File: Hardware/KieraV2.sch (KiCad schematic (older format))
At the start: 19 parts, among them SW1 SW_Rotary1x4, SW2 SW_Rotary1x4, SW3 SW_Push, SW4 SW_Push, SW5 SW_Push

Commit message: added .gitignore, SW_rotary_2x4
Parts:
- removed SW1, SW2: SW_Rotary1x4, symbol Switch:SW_Rotary1x4
- added J1: Conn_01x06_Male, symbol Connector:Conn_01x06_Male
- added SW1, SW2: SW_Rotary2x4, symbol Switch:SW_Rotary2x4
- R1, R6: value 56 -> 150
- R2, R7: value 330 -> 680
- R3, R8: value 680 -> 1k97
- R4, R9: value 2k7 -> 22k
- U?: symbol STM32L4P5RET6:STM32L4P5RET6 -> KieraV2-rescue:STM32L4P5RET6-STM32L4P5RET6
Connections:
- net labels added: TODO
- wire segments 55 -> 63
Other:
- moved on the sheet: R1, R10, R11, R12, R13, R2, R3, R4, R5, R6, R7, R8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

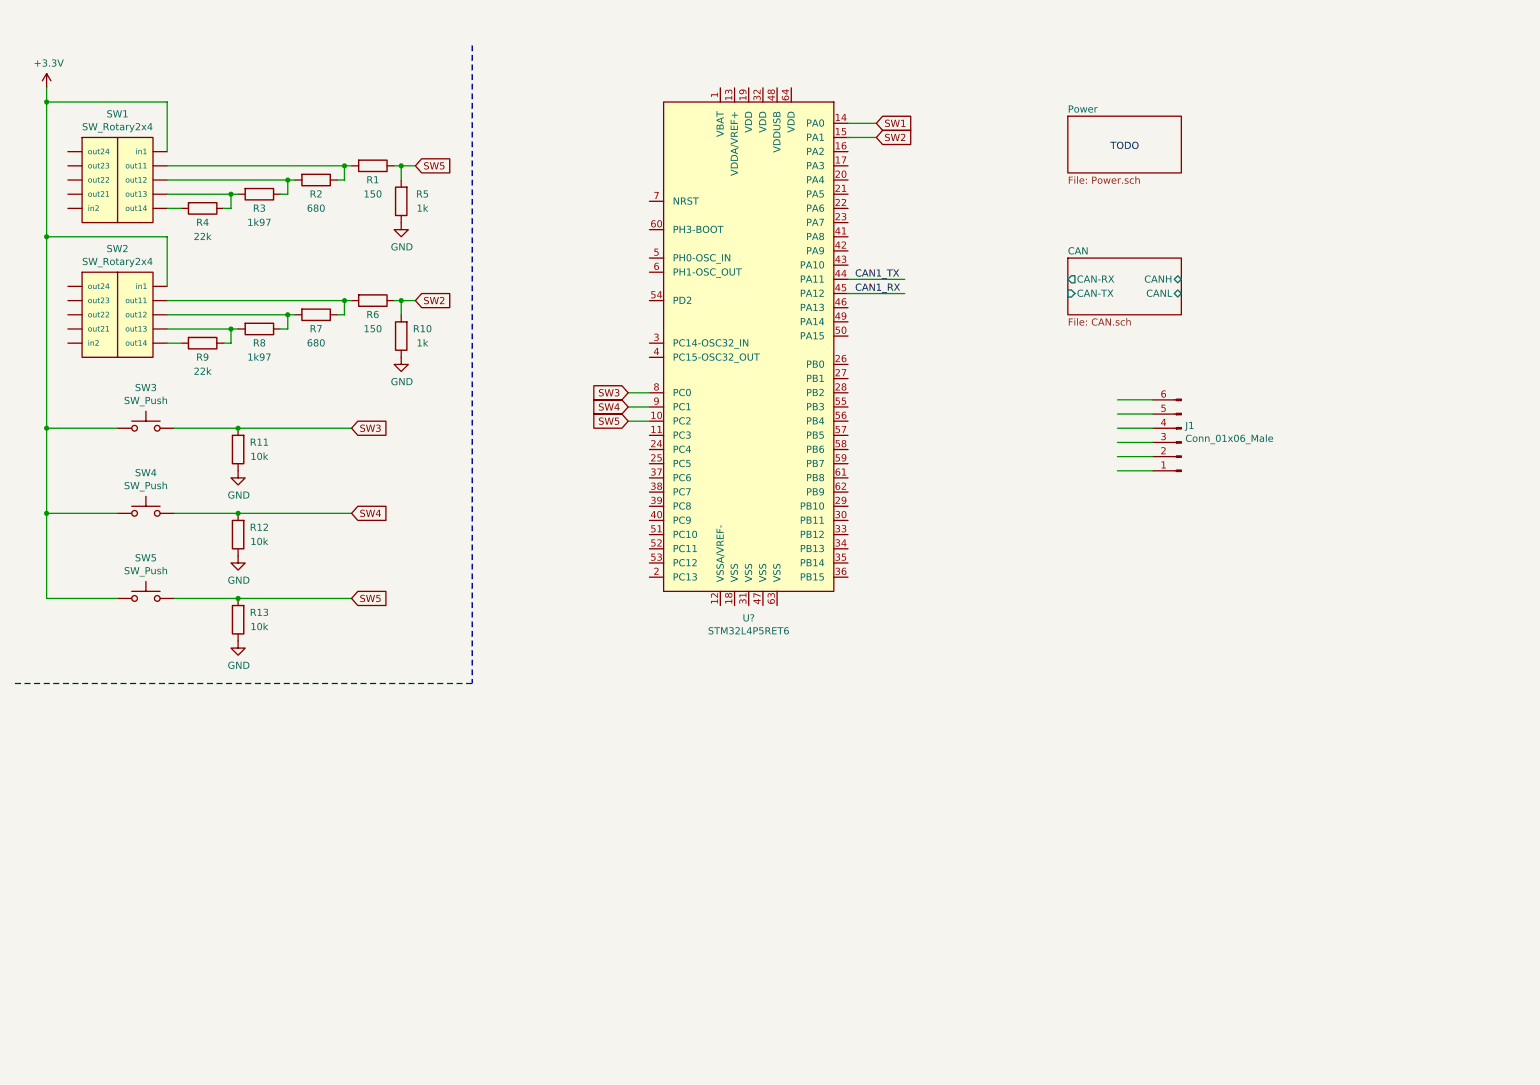
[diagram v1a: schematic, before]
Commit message: added SWD pinout
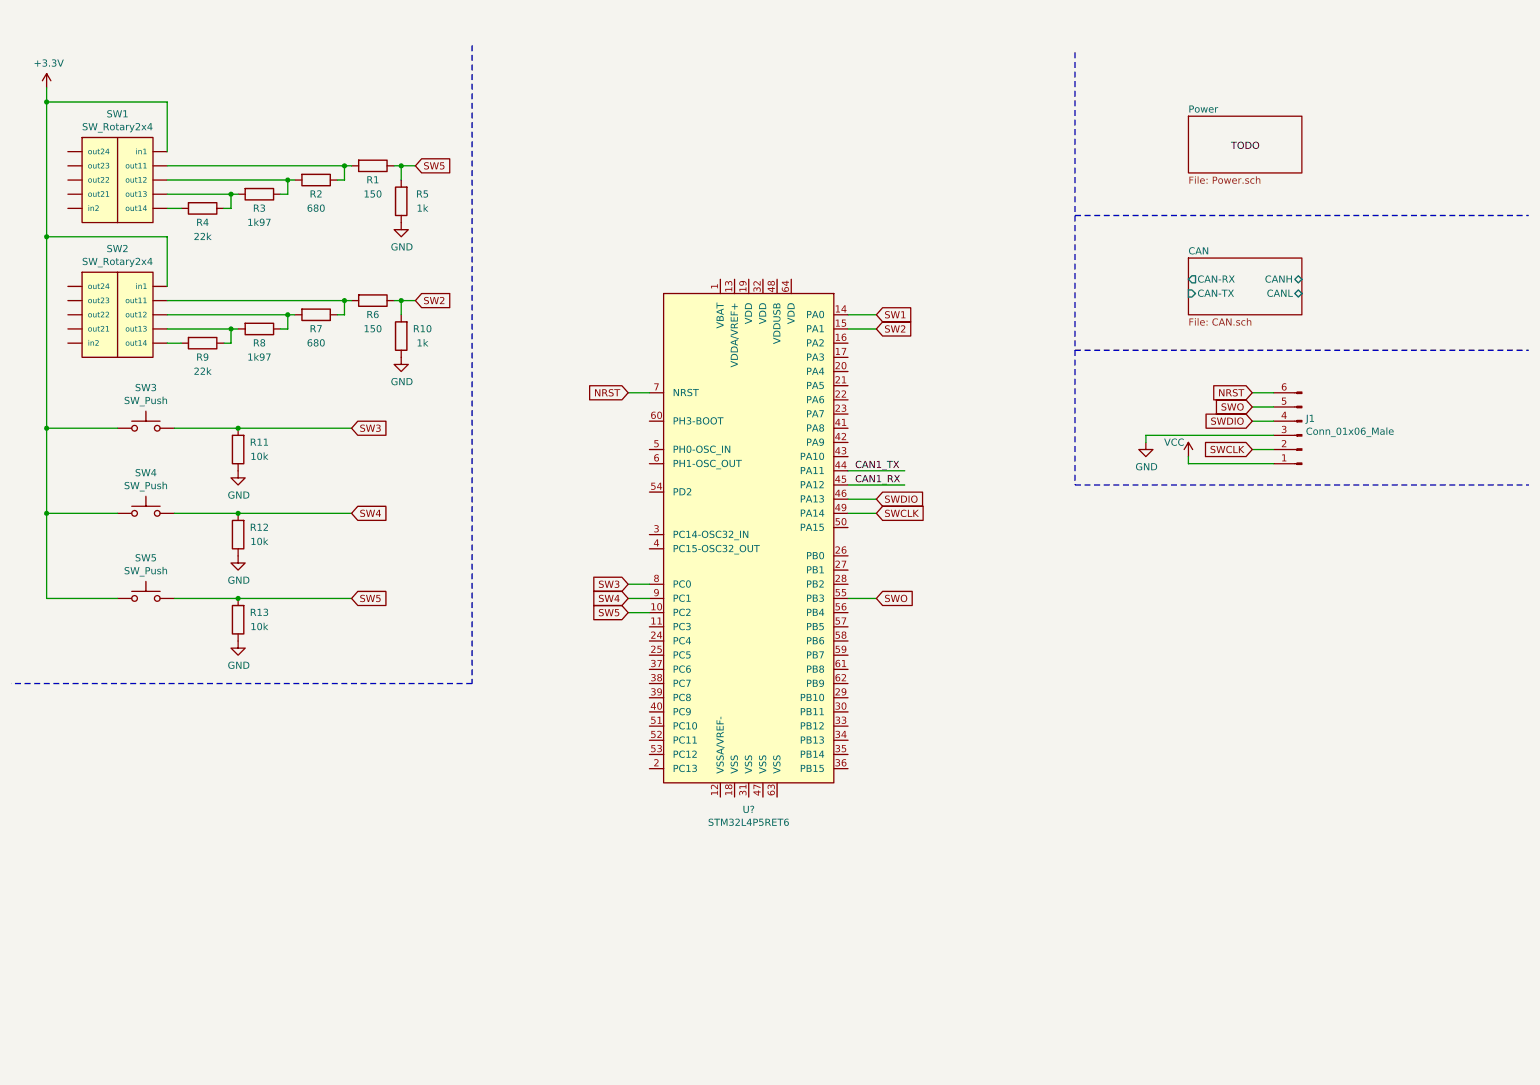
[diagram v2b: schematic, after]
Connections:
- net labels added: NRST, SWCLK, SWDIO, SWO, VCC
- wire segments 63 -> 69
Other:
- moved on the sheet: J1, U?
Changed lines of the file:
@@
 L KieraV2-rescue:STM32L4P5RET6-STM32L4P5RET6 U?
 U 1 1 619BCA75
-P 5700 2550
-F 0 "U?" H 5700 561 50  0000 C CNN
-F 1 "STM32L4P5RET6" H 5700 470 50  0000 C CNN
-F 2 "Package_QFP:LQFP-64_10x10mm_P0.5mm" H 5700 350 50  0001 C CNN
-F 3 "https://www.st.com/en/microcontrollers-microprocessors/stm32l4p5re.html#documentation" H 5700 350 50  0001 C CNN
-	1    5700 2550
+P 5700 3900
+F 0 "U?" H 5700 1911 50  0000 C CNN
+F 1 "STM32L4P5RET6" H 5700 1820 50  0000 C CNN
+F 2 "Package_QFP:LQFP-64_10x10mm_P0.5mm" H 5700 1700 50  0001 C CNN
+F 3 "https://www.st.com/en/microcontrollers-microprocessors/stm32l4p5re.html#documentation" H 5700 1700 50  0001 C CNN
+	1    5700 3900
 	1    0    0    -1
 $EndComp
@@
 	750  3200 750  3800
 Wire Wire Line
-	5000 2950 4850 2950
-Wire Wire Line
-	5000 3050 4850 3050
-Wire Wire Line
-	5000 3150 4850 3150
-Wire Wire Line
-	6400 1050 6600 1050
-Wire Wire Line
-	6400 1150 6600 1150
-Text GLabel 6600 1050 2    50   Input ~ 0
+	5000 4300 4850 4300
+Wire Wire Line
+	5000 4400 4850 4400
+Wire Wire Line
+	5000 4500 4850 4500
+Wire Wire Line
+	6400 2400 6600 2400
+Wire Wire Line
+	6400 2500 6600 2500
+Text GLabel 6600 2400 2    50   Input ~ 0
 SW1
-Text GLabel 6600 1150 2    50   Input ~ 0
+Text GLabel 6600 2500 2    50   Input ~ 0
 SW2
-Text GLabel 4850 2950 0    50   Input ~ 0
+Text GLabel 4850 4300 0    50   Input ~ 0
 SW3
-Text GLabel 4850 3050 0    50   Input ~ 0
+Text GLabel 4850 4400 0    50   Input ~ 0
 SW4
-Text GLabel 4850 3150 0    50   Input ~ 0
+Text GLabel 4850 4500 0    50   Input ~ 0
 SW5
 Text GLabel 2900 4400 2    50   Input ~ 0
@@
 Connection ~ 2100 3800
 $Sheet
-S 7950 2000 800  400
+S 8800 2000 800  400
 U 61B35764
 F0 "CAN" 50
 F1 "CAN.sch" 50
-F2 "CAN-RX" O L 7950 2150 50
-F3 "CAN-TX" I L 7950 2250 50
-F4 "CANH" B R 8750 2150 50
-F5 "CANL" B R 8750 2250 50
+F2 "CAN-RX" O L 8800 2150 50
+F3 "CAN-TX" I L 8800 2250 50
+F4 "CANH" B R 9600 2150 50
+F5 "CANL" B R 9600 2250 50
 $EndSheet
-Text Label 6450 2150 0    50   ~ 0
+Text Label 6450 3500 0    50   ~ 0
 CAN1_TX
-Text Label 6450 2250 0    50   ~ 0
+Text Label 6450 3600 0    50   ~ 0
 CAN1_RX
 Wire Wire Line
-	6400 2250 6800 2250
-Wire Wire Line
-	6400 2150 6800 2150
+	6400 3600 6800 3600
+Wire Wire Line
+	6400 3500 6800 3500
 $Comp
 L Switch:SW_Rotary2x4 SW1
@@
 	3750 5000 500  5000
 $Sheet
-S 7950 1000 800  400
+S 8800 1000 800  400
 U 61A6380E
 F0 "Power" 50
 F1 "Power.sch" 50
 $EndSheet
-Text Label 8250 1250 0    50   ~ 0
+Text Label 9100 1250 0    50   ~ 0
 TODO
 $Comp
 L Connector:Conn_01x06_Male J1
 U 1 1 61A68069
-P 8750 3300
-F 0 "J1" H 8722 3182 50  0000 R CNN
-F 1 "Conn_01x06_Male" H 8722 3273 50  0000 R CNN
-F 2 "" H 8750 3300 50  0001 C CNN
-F 3 "~" H 8750 3300 50  0001 C CNN
-	1    8750 3300
+P 9600 3250
+F 0 "J1" H 9572 3132 50  0000 R CNN
+F 1 "Conn_01x06_Male" H 9572 3223 50  0000 R CNN
+F 2 "" H 9600 3250 50  0001 C CNN
+F 3 "~" H 9600 3250 50  0001 C CNN
+	1    9600 3250
 	-1   0    0    1
 $EndComp
 Wire Wire Line
-	8550 3000 8300 3000
-Wire Wire Line
-	8550 3100 8300 3100
-Wire Wire Line
-	8550 3200 8300 3200
-Wire Wire Line
-	8550 3300 8300 3300
-Wire Wire Line
-	8550 3400 8300 3400
-Wire Wire Line
-	8550 3500 8300 3500
+	4850 2950 5000 2950
+Text GLabel 4850 2950 0    50   Input ~ 0
+NRST
+Wire Wire Line
+	6400 3800 6600 3800
+Text GLabel 6600 3800 2    50   Input ~ 0
+SWCLK
+Wire Wire Line
+	6400 3700 6600 3700
+Text GLabel 6600 3700 2    50   Input ~ 0
+SWDIO
+Wire Wire Line
+	6400 4400 6600 4400
+Text GLabel 6600 4400 2    50   Input ~ 0
+SWO
+Text GLabel 9250 3050 0    50   Input ~ 0
+SWO
+Text GLabel 9250 3150 0    50   Input ~ 0
+SWDIO
+Text GLabel 9250 2950 0    50   Input ~ 0
+NRST
+$Comp
+L power:GND #PWR?
+U 1 1 61A4CEAD
+P 8500 3300
+F 0 "#PWR?" H 8500 3050 50  0001 C CNN
+F 1 "GND" H 8505 3127 50  0000 C CNN
+F 2 "" H 8500 3300 50  0001 C CNN
+F 3 "" H 8500 3300 50  0001 C CNN
+	1    8500 3300
+	1    0    0    -1
+$EndComp
+Text GLabel 9250 3350 0    50   Input ~ 0
+SWCLK
+$Comp
+L power:VCC #PWR?
+U 1 1 61A51913
+P 8800 3400
+F 0 "#PWR?" H 8800 3250 50  0001 C CNN
+F 1 "VCC" H 8700 3500 50  0000 C CNN
+F 2 "" H 8800 3400 50  0001 C CNN
+F 3 "" H 8800 3400 50  0001 C CNN
+	1    8800 3400
+	1    0    0    -1
+$EndComp
+Wire Wire Line
+	8500 3300 8500 3250
+Wire Wire Line
+	8500 3250 9400 3250
+Wire Wire Line
+	8800 3400 8800 3450
+Wire Wire Line
+	8800 3450 9400 3450
+Wire Wire Line
+	9400 3350 9250 3350
+Wire Wire Line
+	9250 3150 9400 3150
+Wire Wire Line
+	9400 3050 9250 3050
+Wire Wire Line
+	9250 2950 9400 2950
+Wire Notes Line
+	8000 550  8000 3600
+Wire Notes Line
+	8000 2650 11200 2650
+Wire Notes Line
+	8000 1700 11200 1700
+Wire Notes Line
+	8000 3600 11200 3600
 $EndSCHEMATC

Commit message: added VSS, connector for can and power
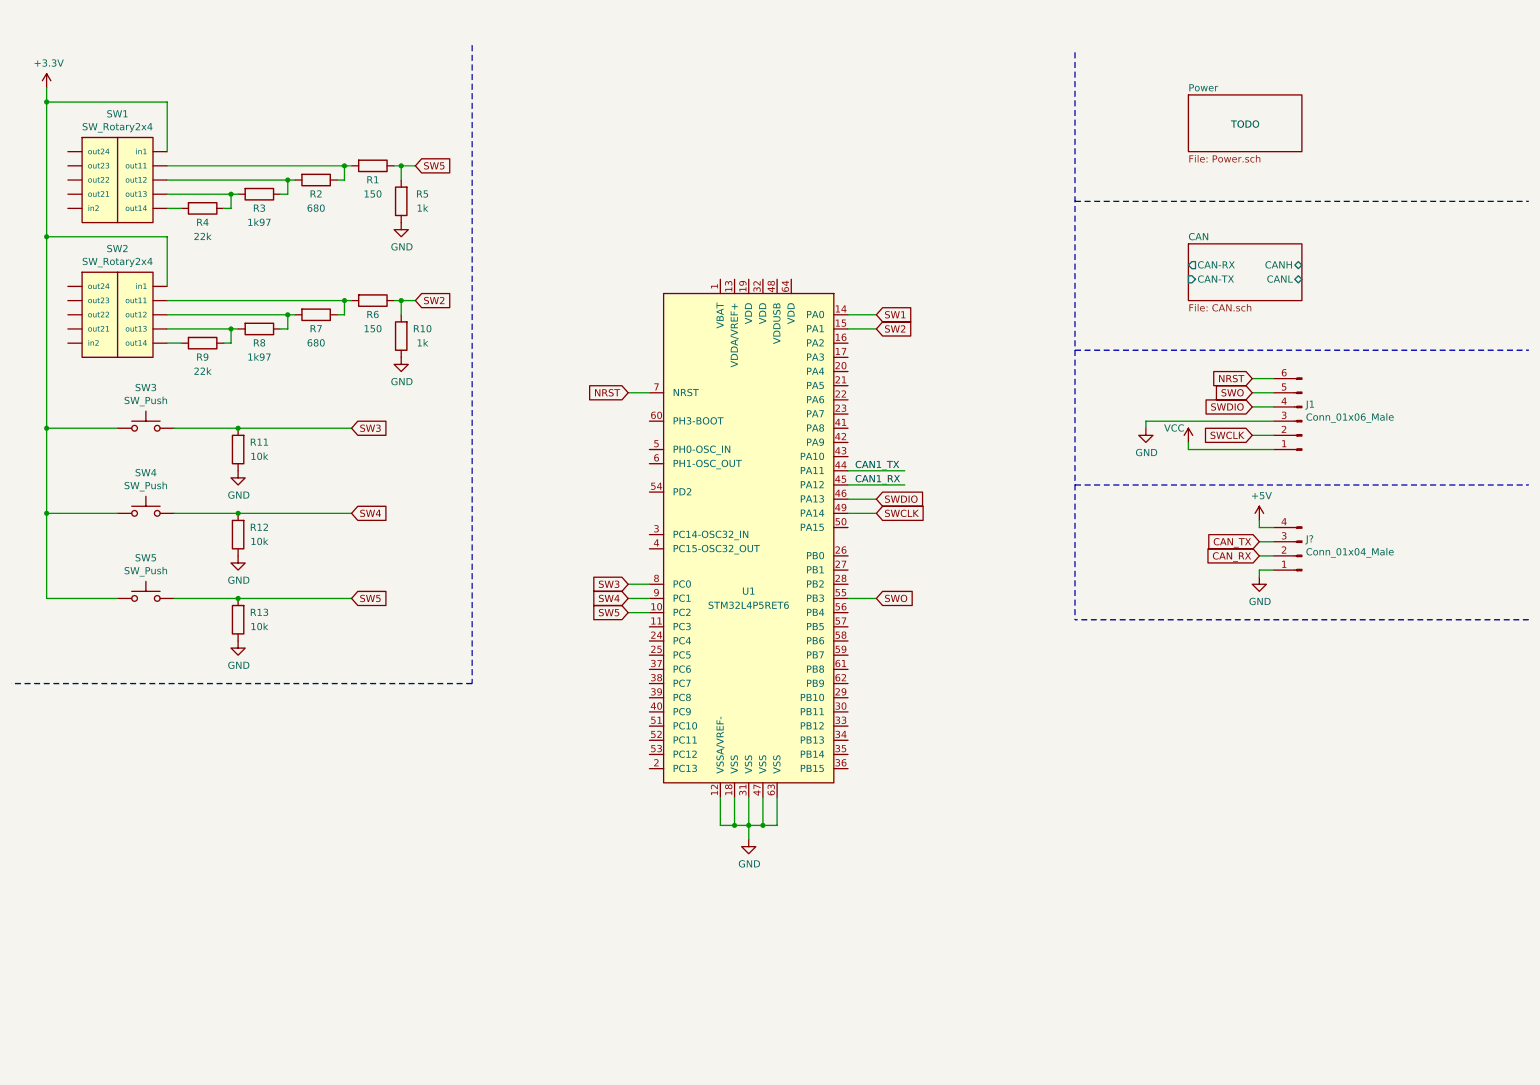
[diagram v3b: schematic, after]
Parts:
- added J?: Conn_01x04_Male, symbol Connector:Conn_01x04_Male
- gave numbers to parts that had none: 1
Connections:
- net GND: now also U1.12 (VSSA/VREF-), U1.18 (VSS), U1.31 (VSS), U1.47 (VSS), U1.63 (VSS), J?.1 (Pin_1)
- new net +5V: J?.4 (Pin_4)
- new net CAN_RX: J?.2 (Pin_2)
- new net CAN_TX: J?.3 (Pin_3)
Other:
- moved on the sheet: J1
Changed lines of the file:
@@
 $EndDescr
 $Comp
-L KieraV2-rescue:STM32L4P5RET6-STM32L4P5RET6 U?
+L KieraV2-rescue:STM32L4P5RET6-STM32L4P5RET6 U1
 U 1 1 619BCA75
 P 5700 3900
-F 0 "U?" H 5700 1911 50  0000 C CNN
-F 1 "STM32L4P5RET6" H 5700 1820 50  0000 C CNN
+F 0 "U1" H 5700 3450 50  0000 C CNN
+F 1 "STM32L4P5RET6" H 5700 3350 50  0000 C CNN
 F 2 "Package_QFP:LQFP-64_10x10mm_P0.5mm" H 5700 1700 50  0001 C CNN
 F 3 "https://www.st.com/en/microcontrollers-microprocessors/stm32l4p5re.html#documentation" H 5700 1700 50  0001 C CNN
@@
 Connection ~ 2100 3800
 $Sheet
-S 8800 2000 800  400
+S 8800 1900 800  400
 U 61B35764
 F0 "CAN" 50
 F1 "CAN.sch" 50
-F2 "CAN-RX" O L 8800 2150 50
-F3 "CAN-TX" I L 8800 2250 50
-F4 "CANH" B R 9600 2150 50
-F5 "CANL" B R 9600 2250 50
+F2 "CAN-RX" O L 8800 2050 50
+F3 "CAN-TX" I L 8800 2150 50
+F4 "CANH" B R 9600 2050 50
+F5 "CANL" B R 9600 2150 50
 $EndSheet
 Text Label 6450 3500 0    50   ~ 0
@@
 	3750 5000 500  5000
 $Sheet
-S 8800 1000 800  400
+S 8800 850  800  400
 U 61A6380E
 F0 "Power" 50
 F1 "Power.sch" 50
 $EndSheet
-Text Label 9100 1250 0    50   ~ 0
+Text Label 9100 1100 0    50   ~ 0
 TODO
 $Comp
 L Connector:Conn_01x06_Male J1
 U 1 1 61A68069
-P 9600 3250
-F 0 "J1" H 9572 3132 50  0000 R CNN
-F 1 "Conn_01x06_Male" H 9572 3223 50  0000 R CNN
-F 2 "" H 9600 3250 50  0001 C CNN
-F 3 "~" H 9600 3250 50  0001 C CNN
-	1    9600 3250
+P 9600 3150
+F 0 "J1" H 9572 3032 50  0000 R CNN
+F 1 "Conn_01x06_Male" H 9572 3123 50  0000 R CNN
+F 2 "" H 9600 3150 50  0001 C CNN
+F 3 "~" H 9600 3150 50  0001 C CNN
+	1    9600 3150
 	-1   0    0    1
 $EndComp
@@
 Text GLabel 6600 4400 2    50   Input ~ 0
 SWO
+Text GLabel 9250 2950 0    50   Input ~ 0
+SWO
 Text GLabel 9250 3050 0    50   Input ~ 0
-SWO
-Text GLabel 9250 3150 0    50   Input ~ 0
 SWDIO
-Text GLabel 9250 2950 0    50   Input ~ 0
+Text GLabel 9250 2850 0    50   Input ~ 0
 NRST
 $Comp
 L power:GND #PWR?
 U 1 1 61A4CEAD
-P 8500 3300
-F 0 "#PWR?" H 8500 3050 50  0001 C CNN
-F 1 "GND" H 8505 3127 50  0000 C CNN
-F 2 "" H 8500 3300 50  0001 C CNN
-F 3 "" H 8500 3300 50  0001 C CNN
-	1    8500 3300
-	1    0    0    -1
-$EndComp
-Text GLabel 9250 3350 0    50   Input ~ 0
+P 8500 3200
+F 0 "#PWR?" H 8500 2950 50  0001 C CNN
+F 1 "GND" H 8505 3027 50  0000 C CNN
+F 2 "" H 8500 3200 50  0001 C CNN
+F 3 "" H 8500 3200 50  0001 C CNN
+	1    8500 3200
+	1    0    0    -1
+$EndComp
+Text GLabel 9250 3250 0    50   Input ~ 0
 SWCLK
 $Comp
 L power:VCC #PWR?
 U 1 1 61A51913
-P 8800 3400
-F 0 "#PWR?" H 8800 3250 50  0001 C CNN
-F 1 "VCC" H 8700 3500 50  0000 C CNN
-F 2 "" H 8800 3400 50  0001 C CNN
-F 3 "" H 8800 3400 50  0001 C CNN
-	1    8800 3400
-	1    0    0    -1
-$EndComp
-Wire Wire Line
-	8500 3300 8500 3250
-Wire Wire Line
-	8500 3250 9400 3250
-Wire Wire Line
-	8800 3400 8800 3450
-Wire Wire Line
-	8800 3450 9400 3450
-Wire Wire Line
-	9400 3350 9250 3350
-Wire Wire Line
-	9250 3150 9400 3150
-Wire Wire Line
-	9400 3050 9250 3050
-Wire Wire Line
-	9250 2950 9400 2950
-Wire Notes Line
-	8000 550  8000 3600
+P 8800 3300
+F 0 "#PWR?" H 8800 3150 50  0001 C CNN
+F 1 "VCC" H 8700 3400 50  0000 C CNN
+F 2 "" H 8800 3300 50  0001 C CNN
+F 3 "" H 8800 3300 50  0001 C CNN
+	1    8800 3300
+	1    0    0    -1
+$EndComp
+Wire Wire Line
+	8500 3200 8500 3150
+Wire Wire Line
+	8500 3150 9400 3150
+Wire Wire Line
+	8800 3300 8800 3350
+Wire Wire Line
+	8800 3350 9400 3350
+Wire Wire Line
+	9400 3250 9250 3250
+Wire Wire Line
+	9250 3050 9400 3050
+Wire Wire Line
+	9400 2950 9250 2950
+Wire Wire Line
+	9250 2850 9400 2850
 Wire Notes Line
 	8000 2650 11200 2650
 Wire Notes Line
-	8000 1700 11200 1700
+	8000 1600 11200 1600
 Wire Notes Line
 	8000 3600 11200 3600
+$Comp
+L power:GND #PWR?
+U 1 1 61A87240
+P 5700 6100
+F 0 "#PWR?" H 5700 5850 50  0001 C CNN
+F 1 "GND" H 5705 5927 50  0000 C CNN
+F 2 "" H 5700 6100 50  0001 C CNN
+F 3 "" H 5700 6100 50  0001 C CNN
+	1    5700 6100
+	1    0    0    -1
+$EndComp
+Wire Wire Line
+	5500 5800 5500 6000
+Wire Wire Line
+	5500 6000 5600 6000
+Wire Wire Line
+	5600 5800 5600 6000
+Connection ~ 5600 6000
+Wire Wire Line
+	5600 6000 5700 6000
+Wire Wire Line
+	5700 5800 5700 6000
+Connection ~ 5700 6000
+Wire Wire Line
+	5800 5800 5800 6000
+Wire Wire Line
+	5800 6000 5700 6000
+Wire Wire Line
+	5900 5800 5900 6000
+Wire Wire Line
+	5900 6000 5800 6000
+Connection ~ 5800 6000
+Wire Wire Line
+	5700 6000 5700 6100
+$Comp
+L Connector:Conn_01x04_Male J?
+U 1 1 61A93711
+P 9600 4100
+F 0 "J?" H 9572 3982 50  0000 R CNN
+F 1 "Conn_01x04_Male" H 9572 4073 50  0000 R CNN
+F 2 "" H 9600 4100 50  0001 C CNN
+F 3 "~" H 9600 4100 50  0001 C CNN
+	1    9600 4100
+	-1   0    0    1
+$EndComp
+Wire Wire Line
+	9400 3900 9300 3900
+Wire Wire Line
+	9300 3900 9300 3850
+Wire Wire Line
+	9400 4200 9300 4200
+Wire Wire Line
+	9300 4200 9300 4250
+Wire Wire Line
+	9400 4100 9300 4100
+Wire Wire Line
+	9400 4000 9300 4000
+Text GLabel 9300 4000 0    50   Input ~ 0
+CAN_TX
+Text GLabel 9300 4100 0    50   Input ~ 0
+CAN_RX
+$Comp
+L power:+5V #PWR?
+U 1 1 61A9DC54
+P 9300 3850
+F 0 "#PWR?" H 9300 3700 50  0001 C CNN
+F 1 "+5V" H 9315 4023 50  0000 C CNN
+F 2 "" H 9300 3850 50  0001 C CNN
+F 3 "" H 9300 3850 50  0001 C CNN
+	1    9300 3850
+	1    0    0    -1
+$EndComp
+$Comp
+L power:GND #PWR?
+U 1 1 61A9F0B3
+P 9300 4250
+F 0 "#PWR?" H 9300 4000 50  0001 C CNN
+F 1 "GND" H 9305 4077 50  0000 C CNN
+F 2 "" H 9300 4250 50  0001 C CNN
+F 3 "" H 9300 4250 50  0001 C CNN
+	1    9300 4250
+	1    0    0    -1
+$EndComp
+Wire Notes Line
+	11200 4550 8000 4550
+Wire Notes Line
+	8000 550  8000 4550
 $EndSCHEMATC

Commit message: power
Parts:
- gave numbers to parts that had none: 1
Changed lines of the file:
@@
 Wire Notes Line
 	3750 5000 500  5000
-$Sheet
-S 8800 850  800  400
-U 61A6380E
-F0 "Power" 50
-F1 "Power.sch" 50
-$EndSheet
-Text Label 9100 1100 0    50   ~ 0
-TODO
 $Comp
 L Connector:Conn_01x06_Male J1
@@
 	5700 6000 5700 6100
 $Comp
-L Connector:Conn_01x04_Male J?
+L Connector:Conn_01x04_Male J2
 U 1 1 61A93711
 P 9600 4100
-F 0 "J?" H 9572 3982 50  0000 R CNN
+F 0 "J2" H 9572 3982 50  0000 R CNN
 F 1 "Conn_01x04_Male" H 9572 4073 50  0000 R CNN
 F 2 "" H 9600 4100 50  0001 C CNN
@@
 Wire Notes Line
 	8000 550  8000 4550
+$Sheet
+S 8800 850  800  400
+U 61A6380E
+F0 "Power" 50
+F1 "Power.sch" 50
+$EndSheet
 $EndSCHEMATC
